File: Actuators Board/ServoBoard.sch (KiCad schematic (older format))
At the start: 28 parts, among them J10 Conn_01x02_Male, J9 Conn_01x02_Male, Q1 MMDT2222A

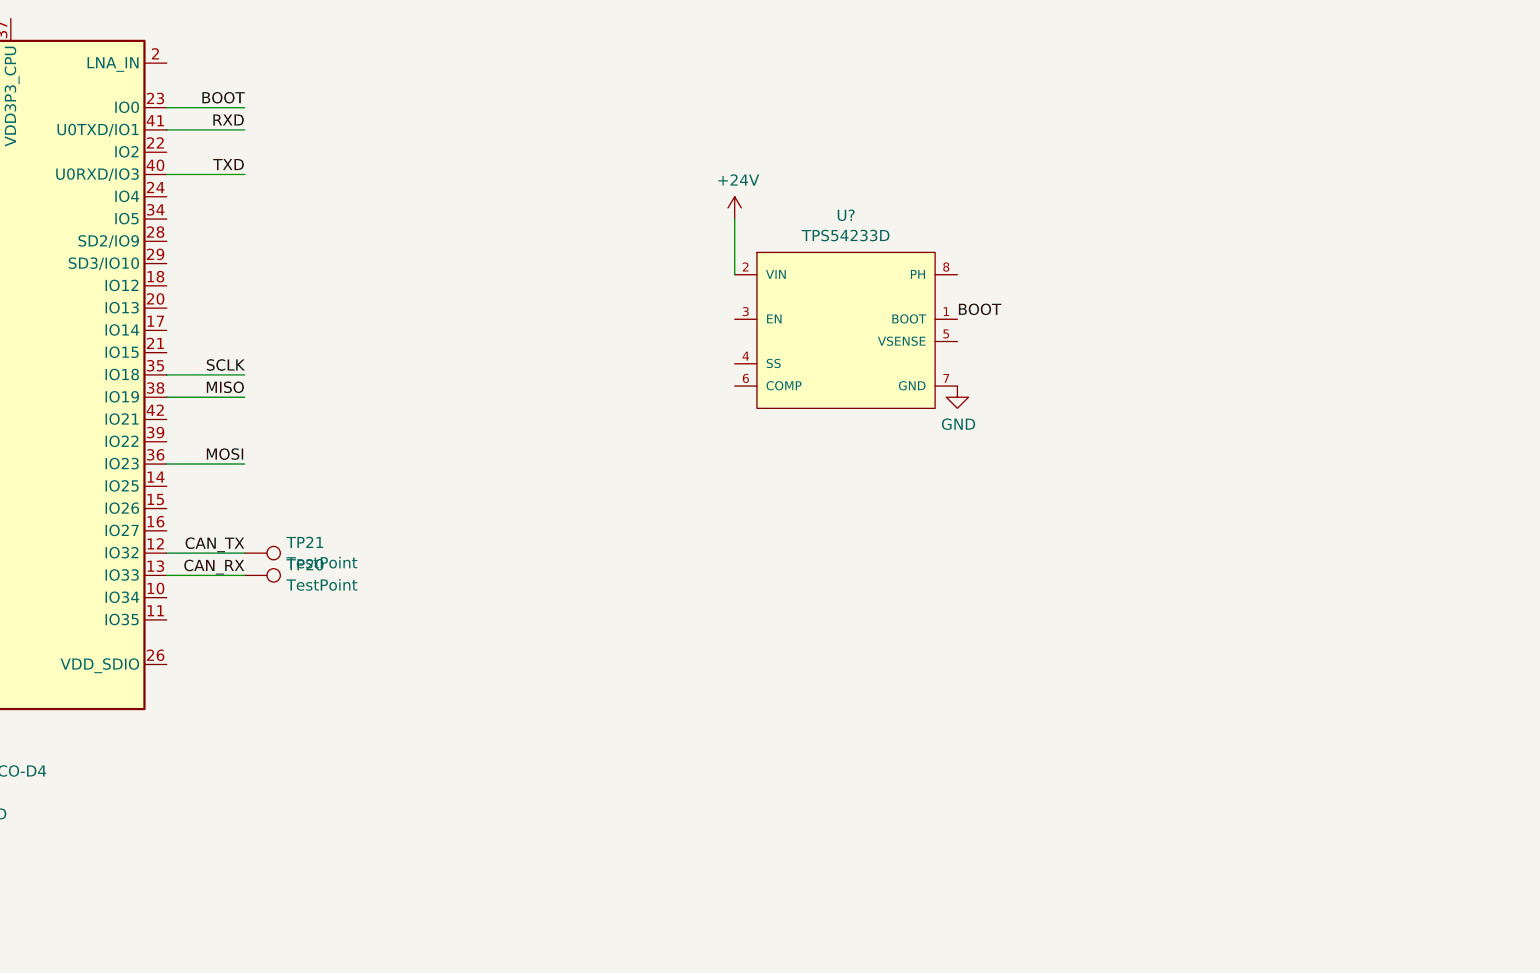
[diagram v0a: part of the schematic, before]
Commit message: Finished buck converter schematic, connected servo
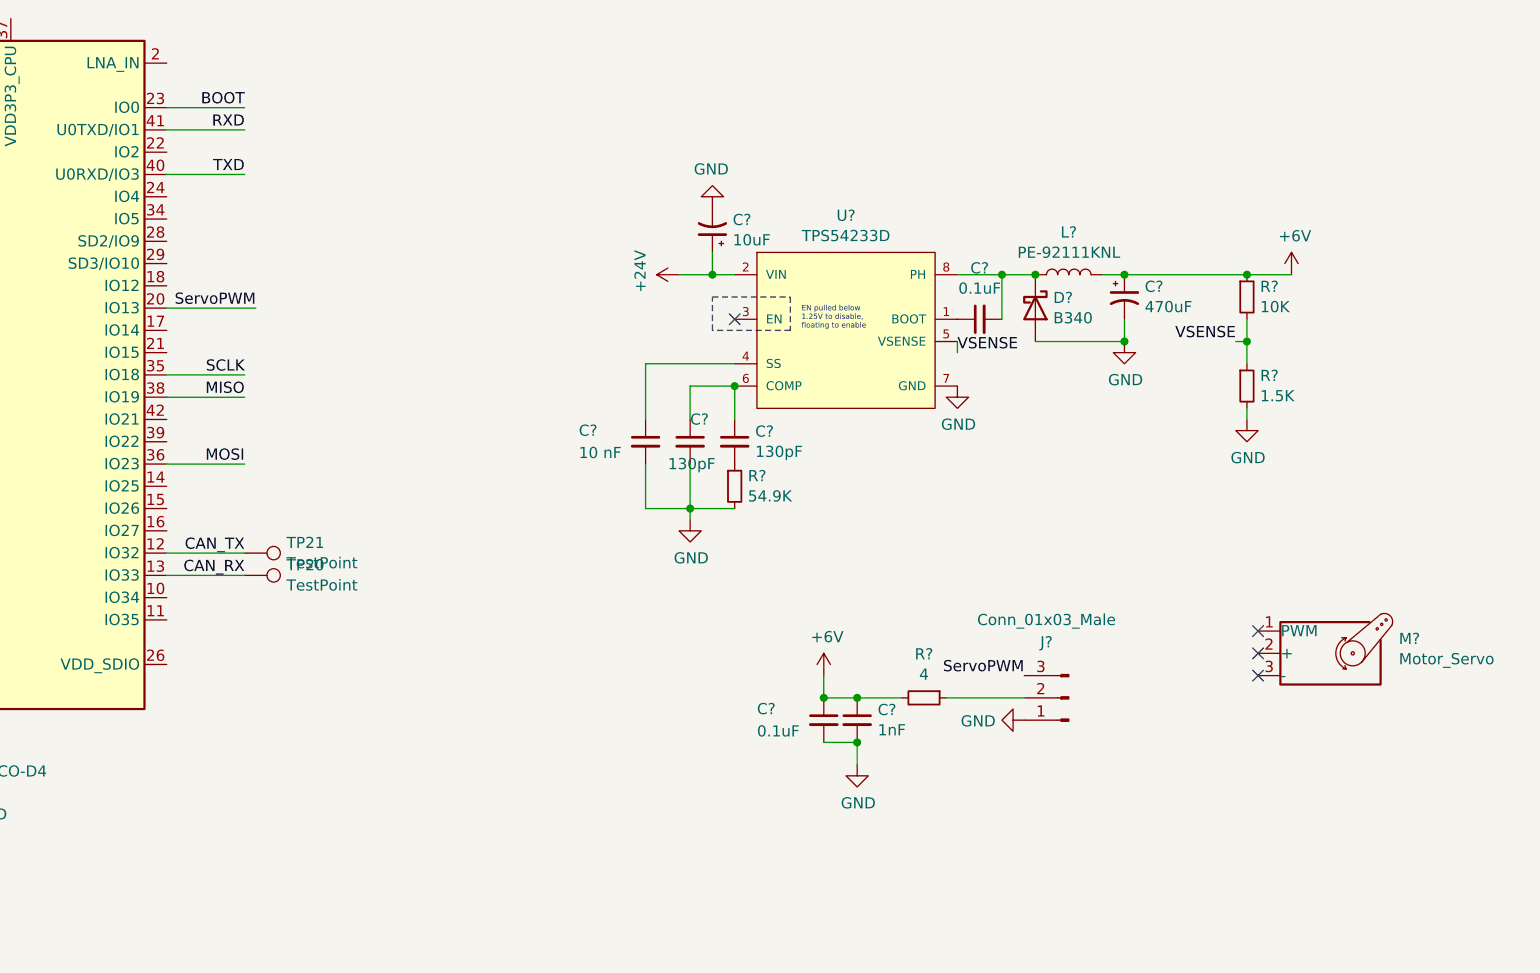
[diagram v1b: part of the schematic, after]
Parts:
- added C? (x2): 0.1uF, symbol Device:C_Small
- added C?: 470uF, symbol Device:CP1_Small
- added C?: 10uF, symbol Device:CP1_Small
- added C? (x2): 130pF, symbol Device:C_Small
- added C?: 10 nF, symbol Device:C_Small
- added C?: 1nF, symbol Device:C_Small
- added D?: B340, Diode_SMD:D_SMC, symbol Diode:B340
- added J?: Conn_01x03_Male, symbol Connector:Conn_01x03_Male
- added L?: PE-92111KNL, symbol Device:L
- added M?: Motor_Servo, symbol Motor:Motor_Servo
- added R?: 54.9K, symbol Device:R_Small
- added R?: 10K, symbol Device:R_Small
- added R?: 1.5K, symbol Device:R_Small
- added R?: 4, symbol Device:R_Small
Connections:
- net +24V: now also C?.1
- net BOOT: no longer U?.1 (BOOT)
- net GND: now also C?.2, C?.2, C?.2, C?.2, C?.2, C?.2, D?.2 (A), J?.1 (Pin_1), R?.2, R?.2
- net ServoPWM: now reaches U?.20 (IO13)
- net ServoPWM: now also J?.3 (Pin_3)
- net at U?.4 (SS): now also C?.1
- net VSENSE: now reaches U?.5 (VSENSE)
- net VSENSE: now also R?.1, R?.2
- net at U?.6 (COMP): now also C?.1, C?.1
- net at U?.8 (PH): now also C?.2, D?.1 (K), L?.1
- new net: C?.1, U?.1 (BOOT)
- new net: C?.2, R?.1
- new net: J?.2 (Pin_2), R?.1
- new net +6V: C?.1, C?.1, C?.1, L?.2, R?.1, R?.2
- no-connect marks 0 -> 4
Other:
- note added: "EN pulled below \n1.25V to disable, \nfloating to enable\n"

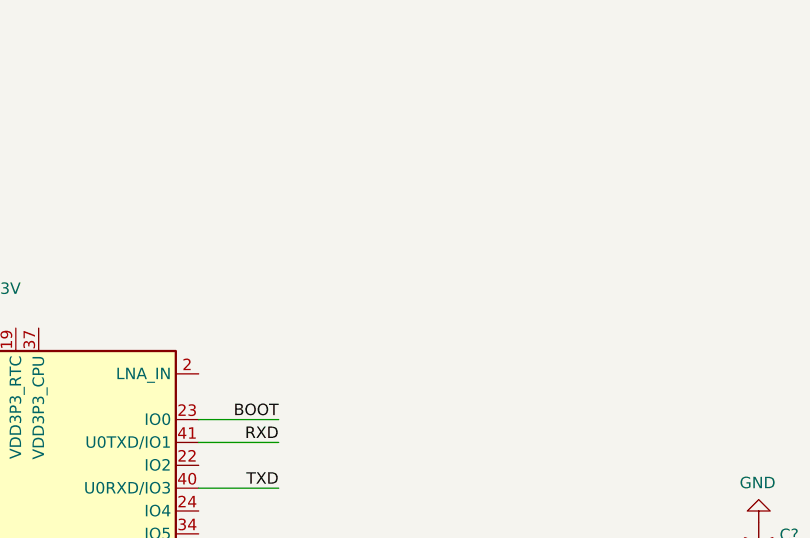
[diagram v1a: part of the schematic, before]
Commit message: Added Rf antenna to all boards
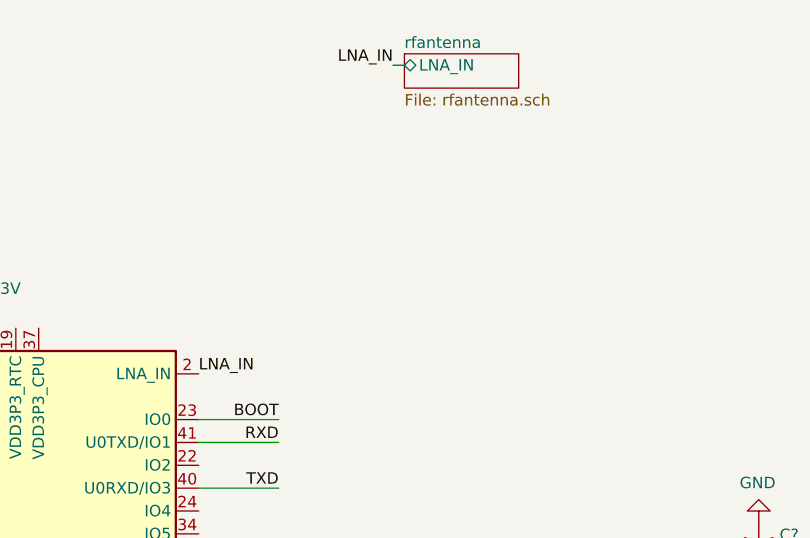
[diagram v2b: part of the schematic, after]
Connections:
- net LNA_IN: now reaches U?.2 (LNA_IN)
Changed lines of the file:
@@
 	1    0    0    -1
 $EndComp
+$Sheet
+S 5900 750  500  150
+U 61A24258
+F0 "rfantenna" 50
+F1 "rfantenna.sch" 50
+F2 "LNA_IN" B L 5900 800 50
+$EndSheet
+Text Label 5850 800  2    50   ~ 0
+LNA_IN
+Wire Wire Line
+	5900 800  5850 800
+Text Label 5000 2150 0    50   ~ 0
+LNA_IN
 $EndSCHEMATC

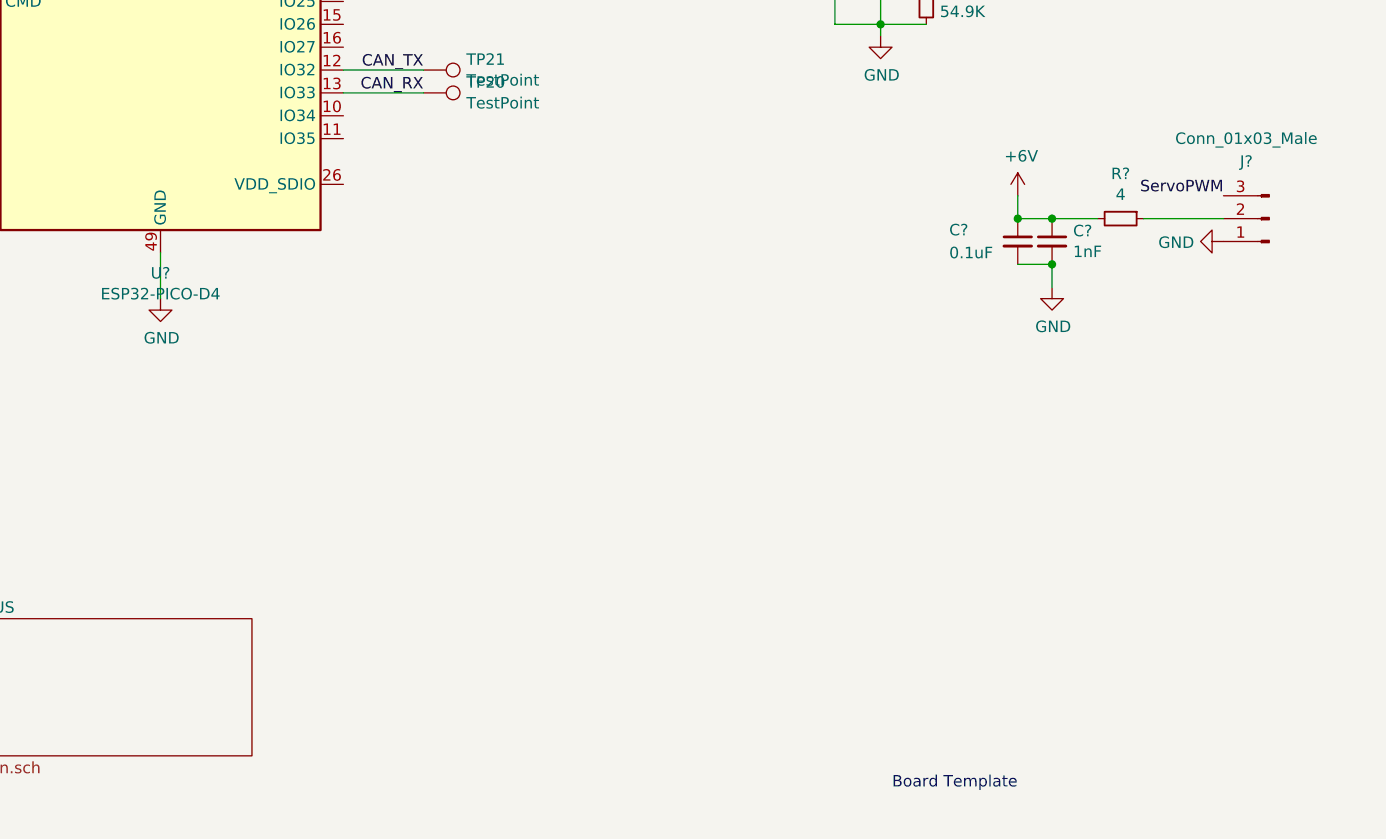
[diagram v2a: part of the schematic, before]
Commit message: Place Hierarchical Pins from CAN sheet to each board.
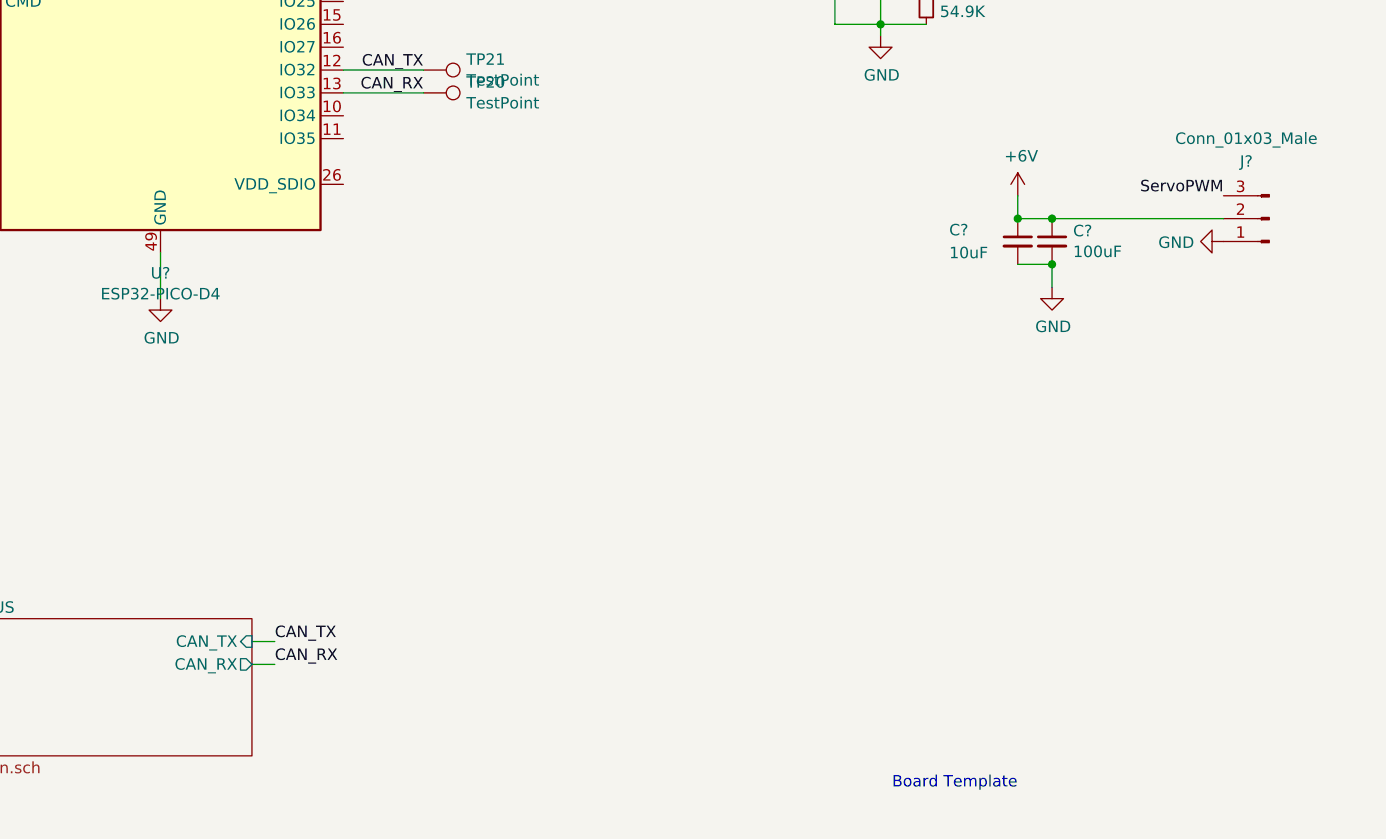
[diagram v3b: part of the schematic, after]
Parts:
- removed R?: 4, symbol Device:R_Small
- C?: value 1nF -> 100uF
- C?: value 0.1uF -> 10uF
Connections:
- net +6V: now also J?.2 (Pin_2)
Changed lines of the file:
@@
 $Descr A4 11693 8268
 encoding utf-8
-Sheet 1 3
+Sheet 1 4
 Title ""
 Date ""
@@
 F0 "CAN-BUS" 50
 F1 "can.sch" 50
+F2 "CAN_TX" I R 4600 6850 50
+F3 "CAN_RX" O R 4600 6950 50
 $EndSheet
 $Comp
@@
 P 8100 5100
 F 0 "C?" H 8192 5146 50  0000 L CNN
-F 1 "1nF" H 8192 5055 50  0000 L CNN
+F 1 "100uF" H 8192 5055 50  0000 L CNN
 F 2 "" H 8100 5100 50  0001 C CNN
 F 3 "~" H 8100 5100 50  0001 C CNN
@@
 P 7950 5100
 F 0 "C?" H 7650 5150 50  0000 L CNN
-F 1 "0.1uF" H 7650 5050 50  0000 L CNN
+F 1 "10uF" H 7650 5050 50  0000 L CNN
 F 2 "" H 7950 5100 50  0001 C CNN
 F 3 "~" H 7950 5100 50  0001 C CNN
@@
 	0    1    1    0
 $EndComp
-$Comp
-L Device:R_Small R?
-U 1 1 61AD9E9D
-P 8400 5000
-F 0 "R?" V 8204 5000 50  0000 C CNN
-F 1 "4" V 8295 5000 50  0000 C CNN
-F 2 "" H 8400 5000 50  0001 C CNN
-F 3 "~" H 8400 5000 50  0001 C CNN
-	1    8400 5000
-	0    1    1    0
-$EndComp
-Wire Wire Line
-	8100 5000 8300 5000
 Connection ~ 8100 5000
-Wire Wire Line
-	8500 5000 8850 5000
 Wire Wire Line
 	7950 5000 7950 4900
@@
 Text Label 5000 2150 0    50   ~ 0
 LNA_IN
+Wire Wire Line
+	4600 6850 4700 6850
+Wire Wire Line
+	4600 6950 4700 6950
+Text Label 4700 6850 0    50   ~ 0
+CAN_TX
+Text Label 4700 6950 0    50   ~ 0
+CAN_RX
+Wire Wire Line
+	8100 5000 8850 5000
 $EndSCHEMATC

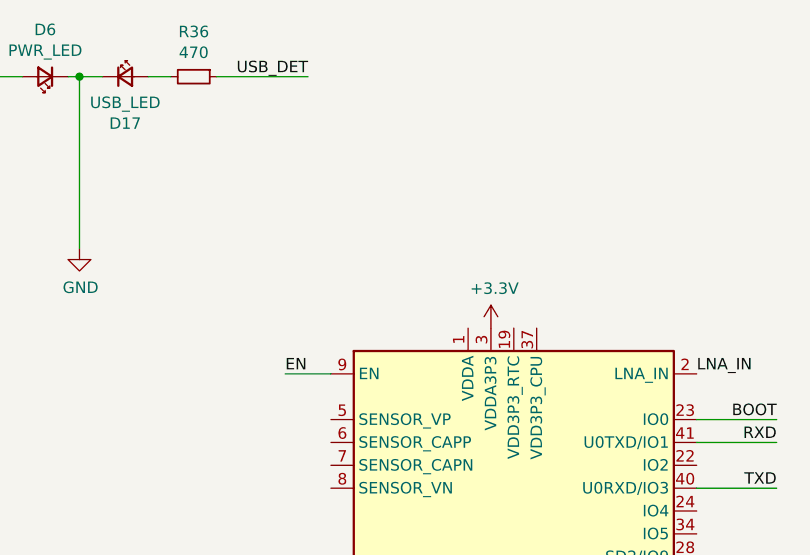
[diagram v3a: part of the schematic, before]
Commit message: Connected 3.3V to ESP32 according to schematic
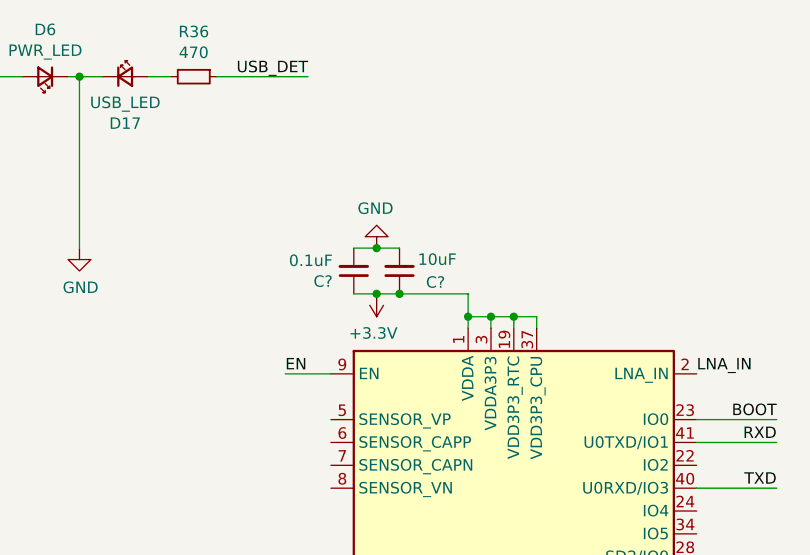
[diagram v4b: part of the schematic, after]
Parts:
- added C?: 10uF, symbol Device:C_Small
- added C?: 0.1uF, symbol Device:C_Small
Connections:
- net +3V3: now also U?.1 (VDDA), U?.19 (VDD3P3_RTC), U?.37 (VDD3P3_CPU), U?.43 (VDDA), U?.46 (VDDA), C?.1, C?.1
- net GND: now also C?.2, C?.2
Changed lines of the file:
@@
 $EndDescr
-$Comp
-L power:+3.3V #PWR020
-U 1 1 5DA60792
-P 4100 1950
-F 0 "#PWR020" H 4100 1800 50  0001 C CNN
-F 1 "+3.3V" H 4115 2123 50  0000 C CNN
-F 2 "" H 4100 1950 50  0001 C CNN
-F 3 "" H 4100 1950 50  0001 C CNN
-	1    4100 1950
-	1    0    0    -1
-$EndComp
 $Comp
 L power:GND #PWR021
@@
 Wire Wire Line
 	8100 5000 8850 5000
+$Comp
+L power:+3.3V #PWR?
+U 1 1 61AA6780
+P 3600 1800
+AR Path="/61AA6780" Ref="#PWR?"  Part="1"
+AR Path="/61AA560B/61AA6780" Ref="#PWR?"  Part="1"
+F 0 "#PWR?" H 3600 1650 50  0001 C CNN
+F 1 "+3.3V" H 3615 1973 50  0000 C CNN
+F 2 "" H 3600 1800 50  0001 C CNN
+F 3 "" H 3600 1800 50  0001 C CNN
+	1    3600 1800
+	-1   0    0    1
+$EndComp
+$Comp
+L Device:C_Small C?
+U 1 1 61AA6786
+P 3700 1700
+AR Path="/61AA6786" Ref="C?"  Part="1"
+AR Path="/61AA560B/61AA6786" Ref="C?"  Part="1"
+F 0 "C?" H 3500 1750 50  0000 L CNN
+F 1 "10uF" H 3450 1650 50  0000 L CNN
+F 2 "" H 3700 1700 50  0001 C CNN
+F 3 "~" H 3700 1700 50  0001 C CNN
+	1    3700 1700
+	-1   0    0    1
+$EndComp
+$Comp
+L Device:C_Small C?
+U 1 1 61AA678C
+P 3500 1700
+AR Path="/61AA678C" Ref="C?"  Part="1"
+AR Path="/61AA560B/61AA678C" Ref="C?"  Part="1"
+F 0 "C?" H 3592 1746 50  0000 L CNN
+F 1 "0.1uF" H 3592 1655 50  0000 L CNN
+F 2 "" H 3500 1700 50  0001 C CNN
+F 3 "~" H 3500 1700 50  0001 C CNN
+	1    3500 1700
+	-1   0    0    1
+$EndComp
+Wire Wire Line
+	3700 1800 3600 1800
+Wire Wire Line
+	3700 1600 3600 1600
+$Comp
+L power:GND #PWR?
+U 1 1 61AA6794
+P 3600 1600
+AR Path="/61AA6794" Ref="#PWR?"  Part="1"
+AR Path="/61AA560B/61AA6794" Ref="#PWR?"  Part="1"
+F 0 "#PWR?" H 3600 1350 50  0001 C CNN
+F 1 "GND" H 3605 1427 50  0000 C CNN
+F 2 "" H 3600 1600 50  0001 C CNN
+F 3 "" H 3600 1600 50  0001 C CNN
+	1    3600 1600
+	-1   0    0    1
+$EndComp
+Connection ~ 3600 1600
+Wire Wire Line
+	3600 1600 3500 1600
+Connection ~ 3600 1800
+Wire Wire Line
+	3600 1800 3500 1800
+Wire Wire Line
+	4000 1900 4100 1900
+Wire Wire Line
+	4100 1900 4100 1950
+Wire Wire Line
+	4000 1900 4000 1950
+Wire Wire Line
+	4100 1900 4200 1900
+Wire Wire Line
+	4200 1900 4200 1950
+Connection ~ 4100 1900
+Wire Wire Line
+	4200 1900 4300 1900
+Wire Wire Line
+	4300 1900 4300 1950
+Connection ~ 4200 1900
+Wire Wire Line
+	3700 1800 4000 1800
+Wire Wire Line
+	4000 1800 4000 1900
+Connection ~ 3700 1800
+Connection ~ 4000 1900
 $EndSCHEMATC
